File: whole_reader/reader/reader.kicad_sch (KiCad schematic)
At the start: 66 parts, among them U1 LM386, U2 STM32F103C8T6, U3 MCP16301Hx-xCH, U4 MAX3232, Y1 16MHz

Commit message: changed diodes
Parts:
- removed D5, D6: BAT60A, Diode_SMD:D_SOD-323, symbol Diode:BAT60A
- added D5, D6: BAT54J, Diode_SMD:D_SOD-323F, symbol Diode:BAT54J
- D1: value BAT60A -> BAT54J; footprint Diode_SMD:D_SOD-323 -> Diode_SMD:D_SOD-323F
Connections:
- net BOOT0: now also D6.1 (K)
- net V+: now also D5.1 (K)
- net at RJ12.6: now also D6.2 (A)
- net at RJ12.2: now also D5.2 (A)
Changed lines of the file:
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@@
 	(wire
 		(pts
+			(xy 233.68 46.99) (xy 233.68 54.61)
+		)
+		(stroke
+			(width 0)
+			(type default)
+		)
+	)
+	(wire
+		(pts
 			(xy 176.53 130.81) (xy 176.53 134.62)
 		)
@@
 	(wire
 		(pts
-			(xy 233.68 46.99) (xy 233.68 54.61)
-		)
-		(stroke
-			(width 0)
-			(type default)
-		)
-	)
-	(wire
-		(pts
 			(xy 39.37 97.79) (xy 49.53 97.79)
 		)
@@
 	(wire
 		(pts
+			(xy 254 64.77) (xy 255.27 64.77)
+		)
+		(stroke
+			(width 0)
+			(type default)
+		)
+	)
+	(wire
+		(pts
 			(xy 172.72 147.32) (xy 172.72 132.08)
 		)
@@
 	(wire
 		(pts
-			(xy 255.27 64.77) (xy 254 64.77)
-		)
-		(stroke
-			(width 0)
-			(type default)
-		)
-	)
-	(wire
-		(pts
 			(xy 247.65 99.06) (xy 247.65 105.41)
 		)
@@
 	)
 	(symbol
+		(lib_id "Diode:BAT54J")
+		(at 233.68 43.18 270)
+		(unit 1)
+		(exclude_from_sim no)
+		(in_bom yes)
+		(on_board yes)
+		(dnp no)
+		(fields_autoplaced yes)
+		(property "Reference" "D5"
+			(at 236.22 41.5924 90)
+			(effects
+				(font
+					(size 1.27 1.27)
+				)
+				(justify left)
+			)
+		)
+		(property "Value" "BAT54J"
+			(at 236.22 44.1324 90)
+			(effects
+				(font
+					(size 1.27 1.27)
+				)
+				(justify left)
+			)
+		)
+		(property "Footprint" "Diode_SMD:D_SOD-323F"
+			(at 229.235 43.18 0)
+			(effects
+				(font
+					(size 1.27 1.27)
+				)
+				(hide yes)
+			)
+		)
+		(property "Datasheet" "https://assets.nexperia.com/documents/data-sheet/BAT54J.pdf"
+			(at 233.68 43.18 0)
+			(effects
+				(font
+					(size 1.27 1.27)
+				)
+				(hide yes)
+			)
+		)
+		(property "Description" "30V 200mA Schottky diode, SOD-323F"
+			(at 233.68 43.18 0)
+			(effects
+				(font
+					(size 1.27 1.27)
+				)
+				(hide yes)
+			)
+		)
+		(pin "2"
+		)
+		(pin "1"
+		)
+		(instances
+			(project ""
+				(path "/6275a1a7-d424-4390-b849-2e49b1a9780b"
+					(reference "D5")
+					(unit 1)
+				)
+			)
+		)
+	)
+	(symbol
 		(lib_id "power:GND")
 		(at 68.58 67.31 0)
@@
 	)
 	(symbol
-		(lib_id "Diode:BAT54J")
-		(at 140.97 132.08 0)
-		(unit 1)
-		(exclude_from_sim no)
-		(in_bom yes)
-		(on_board yes)
-		(dnp no)
-		(property "Reference" "D1"
-			(at 144.272 130.556 0)
-			(effects
-				(font
-					(size 1.27 1.27)
-				)
-			)
-		)
-		(property "Value" "BAT60A"
-			(at 140.6525 128.27 0)
-			(effects
-				(font
-					(size 1.27 1.27)
-				)
-			)
-		)
-		(property "Footprint" "Diode_SMD:D_SOD-323"
-			(at 140.97 136.525 0)
-			(effects
-				(font
-					(size 1.27 1.27)
-				)
-				(hide yes)
-			)
-		)
-		(property "Datasheet" "https://assets.nexperia.com/documents/data-sheet/BAT54J.pdf"
-			(at 140.97 132.08 0)
-			(effects
-				(font
-					(size 1.27 1.27)
-				)
-				(hide yes)
-			)
-		)
-		(property "Description" "30V 200mA Schottky diode, SOD-323F"
-			(at 140.97 132.08 0)
-			(effects
-				(font
-					(size 1.27 1.27)
-				)
-				(hide yes)
-			)
-		)
-		(property "Note" ""
-			(at 140.97 132.08 0)
-			(effects
-				(font
-					(size 1.27 1.27)
-				)
-			)
-		)
-		(pin "1"
-		)
-		(pin "2"
-		)
-		(instances
-			(project "reader"
-				(path "/6275a1a7-d424-4390-b849-2e49b1a9780b"
-					(reference "D1")
-					(unit 1)
-				)
-			)
-		)
-	)
-	(symbol
 		(lib_id "Device:R")
 		(at 41.91 31.75 0)
@@
 	)
 	(symbol
-		(lib_id "Diode:BAT60A")
-		(at 250.19 64.77 0)
-		(unit 1)
-		(exclude_from_sim no)
-		(in_bom yes)
-		(on_board yes)
-		(dnp no)
-		(property "Reference" "D6"
-			(at 250.19 70.612 0)
-			(effects
-				(font
-					(size 1.27 1.27)
-				)
-			)
-		)
-		(property "Value" "BAT60A"
-			(at 250.19 68.072 0)
-			(effects
-				(font
-					(size 1.27 1.27)
-				)
-			)
-		)
-		(property "Footprint" "Diode_SMD:D_SOD-323"
-			(at 250.19 69.215 0)
-			(effects
-				(font
-					(size 1.27 1.27)
-				)
-				(hide yes)
-			)
-		)
-		(property "Datasheet" "https://www.infineon.com/dgdl/Infineon-BAT60ASERIES-DS-v01_01-en.pdf?fileId=db3a304313d846880113def70c9304a9"
-			(at 250.19 64.77 0)
-			(effects
-				(font
-					(size 1.27 1.27)
-				)
-				(hide yes)
-			)
-		)
-		(property "Description" "10V 3A High Current Recitifier Schottky Diode, SOD-323"
-			(at 250.19 64.77 0)
-			(effects
-				(font
-					(size 1.27 1.27)
-				)
-				(hide yes)
-			)
-		)
-		(property "Note" ""
-			(at 250.19 64.77 0)
-			(effects
-				(font
-					(size 1.27 1.27)
-				)
-			)
-		)
-		(pin "2"
-		)
-		(pin "1"
-		)
-		(instances
-			(project "reader"
-				(path "/6275a1a7-d424-4390-b849-2e49b1a9780b"
-					(reference "D6")
-					(unit 1)
-				)
-			)
-		)
-	)
-	(symbol
 		(lib_id "power:GND")
 		(at 105.41 102.87 0)
@@
 	)
 	(symbol
-		(lib_id "Diode:BAT60A")
-		(at 233.68 43.18 270)
+		(lib_id "Diode:BAT54J")
+		(at 140.97 132.08 0)
 		(unit 1)
 		(exclude_from_sim no)
@@
 		(dnp no)
 		(fields_autoplaced yes)
-		(property "Reference" "D5"
-			(at 236.22 41.5924 90)
+		(property "Reference" "D1"
+			(at 140.6525 125.73 0)
 			(effects
 				(font
 					(size 1.27 1.27)
 				)
-				(justify left)
 			)
 		)
-		(property "Value" "BAT60A"
-			(at 236.22 44.1324 90)
+		(property "Value" "BAT54J"
+			(at 140.6525 128.27 0)
 			(effects
 				(font
 					(size 1.27 1.27)
 				)
-				(justify left)
 			)
 		)
-		(property "Footprint" "Diode_SMD:D_SOD-323"
-			(at 229.235 43.18 0)
+		(property "Footprint" "Diode_SMD:D_SOD-323F"
+			(at 140.97 136.525 0)
 			(effects
 				(font
@@
 			)
 		)
-		(property "Datasheet" "https://www.infineon.com/dgdl/Infineon-BAT60ASERIES-DS-v01_01-en.pdf?fileId=db3a304313d846880113def70c9304a9"
-			(at 233.68 43.18 0)
+		(property "Datasheet" "https://assets.nexperia.com/documents/data-sheet/BAT54J.pdf"
+			(at 140.97 132.08 0)
 			(effects
 				(font
@@
 			)
 		)
-		(property "Description" "10V 3A High Current Recitifier Schottky Diode, SOD-323"
-			(at 233.68 43.18 0)
+		(property "Description" "30V 200mA Schottky diode, SOD-323F"
+			(at 140.97 132.08 0)
 			(effects
 				(font
@@
 			)
 		)
-		(property "Note" ""
-			(at 233.68 43.18 0)
-			(effects
-				(font
-					(size 1.27 1.27)
-				)
-			)
-		)
 		(pin "2"
 		)
@@
 		)
 		(instances
-			(project "reader"
+			(project ""
 				(path "/6275a1a7-d424-4390-b849-2e49b1a9780b"
-					(reference "D5")
+					(reference "D1")
 					(unit 1)
 				)
@@
 					(unit 1)
 				)
+			)
+		)
+	)
+	(symbol
+		(lib_id "Diode:BAT54J")
+		(at 250.19 64.77 0)
+		(unit 1)
+		(exclude_from_sim no)
+		(in_bom yes)
+		(on_board yes)
+		(dnp no)
+		(fields_autoplaced yes)
+		(property "Reference" "D6"
+			(at 249.8725 58.42 0)
+			(effects
+				(font
+					(size 1.27 1.27)
+				)
+			)
+		)
+		(property "Value" "BAT54J"
+			(at 249.8725 60.96 0)
+			(effects
+				(font
+					(size 1.27 1.27)
+				)
+			)
+		)
+		(property "Footprint" "Diode_SMD:D_SOD-323F"
+			(at 250.19 69.215 0)
+			(effects
+				(font
+					(size 1.27 1.27)
+				)
+				(hide yes)
+			)
+		)
+		(property "Datasheet" "https://assets.nexperia.com/documents/data-sheet/BAT54J.pdf"
+			(at 250.19 64.77 0)
+			(effects
+				(font
+					(size 1.27 1.27)
+				)
+				(hide yes)
+			)
+		)
+		(property "Description" "30V 200mA Schottky diode, SOD-323F"
+			(at 250.19 64.77 0)
+			(effects
+				(font
+					(size 1.27 1.27)
+				)
+				(hide yes)
+			)
+		)
+		(pin "2"
+		)
+		(pin "1"
+		)
+		(instances
+			(project ""
+				(path "/6275a1a7-d424-4390-b849-2e49b1a9780b"
+					(reference "D6")
+					(unit 1)
+				)

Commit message: added new diodes
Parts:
- removed D1, D5, D6: BAT54J, Diode_SMD:D_SOD-323F, symbol Diode:BAT54J
- removed D4: BAT60A, Diode_SMD:D_SOD-323, symbol Diode:BAT60A
- added D1, D4, D5, D6: PMEG2010ER, Diode_SMD:Nexperia_CFP3_SOD-123W, symbol Device:D_Schottky
- U1: value LM386 -> LM386M-1
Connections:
- net +3.3V: now also D1.2 (A)
- net BOOT0: now also D6.1 (K)
- net V+: now also D1.1 (K), D4.1 (K), D5.1 (K)
- net at RJ12.2: now also D5.2 (A)
- net at USB-C1.A4 (VBUS), USB-C1.A9 (VBUS), USB-C1.B4 (VBUS)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: now also D4.2 (A)
- net at RJ12.6: now also D6.2 (A)

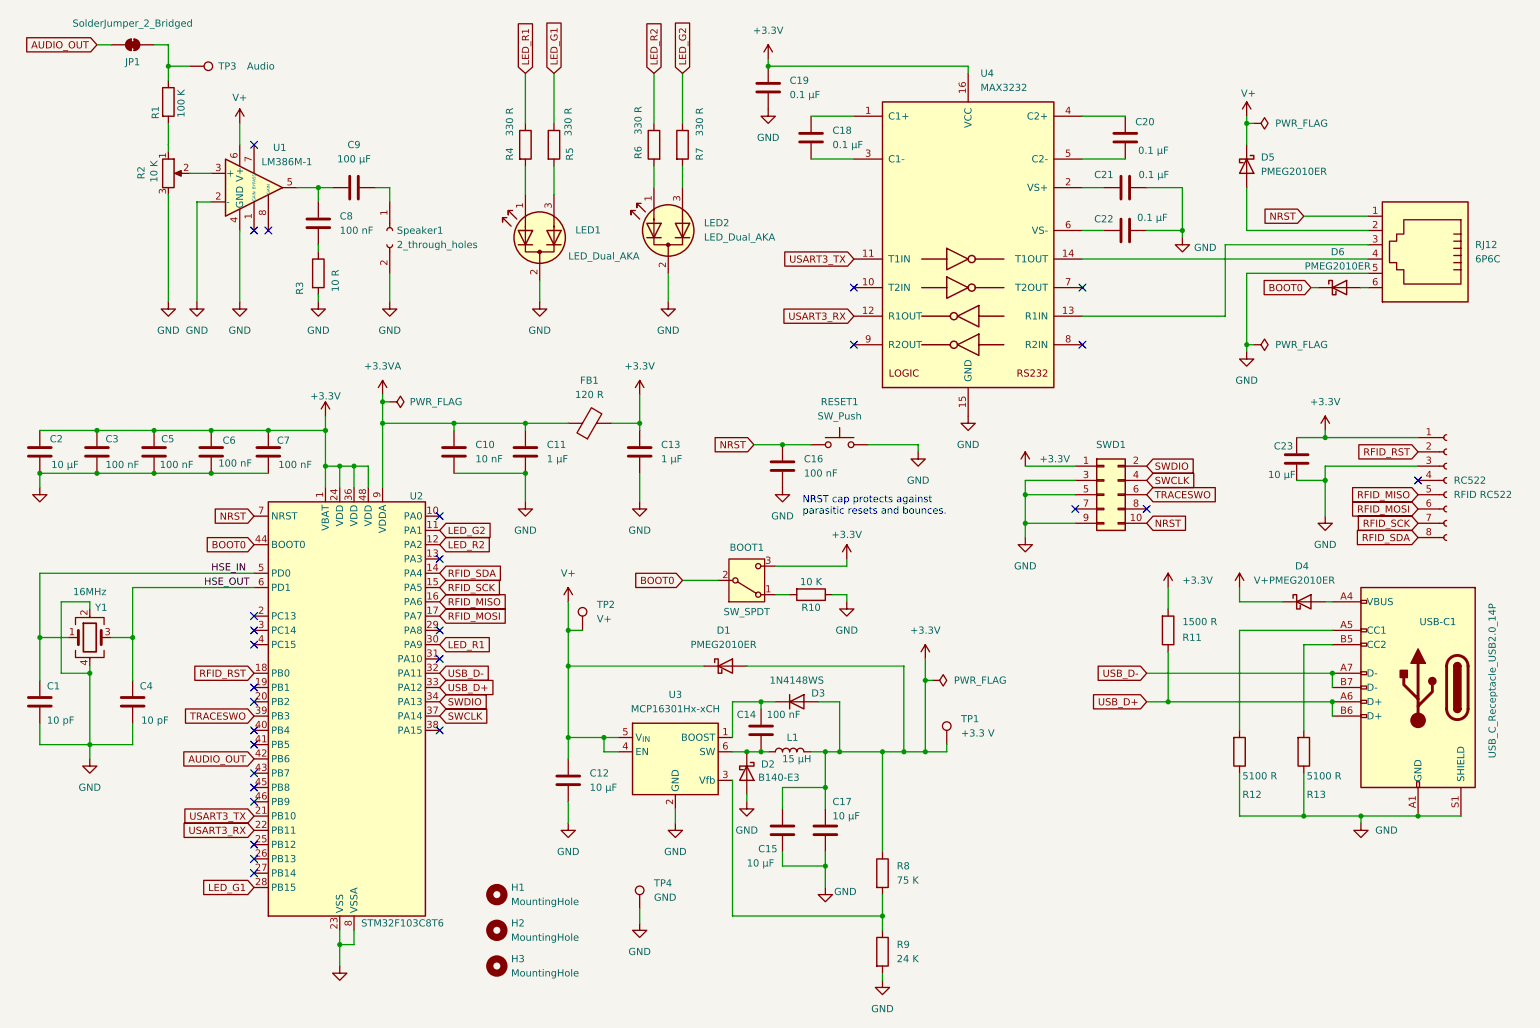
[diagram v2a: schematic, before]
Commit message: Úprava rozloženia dosky a pridanie TP5 pre RFID_IRQ
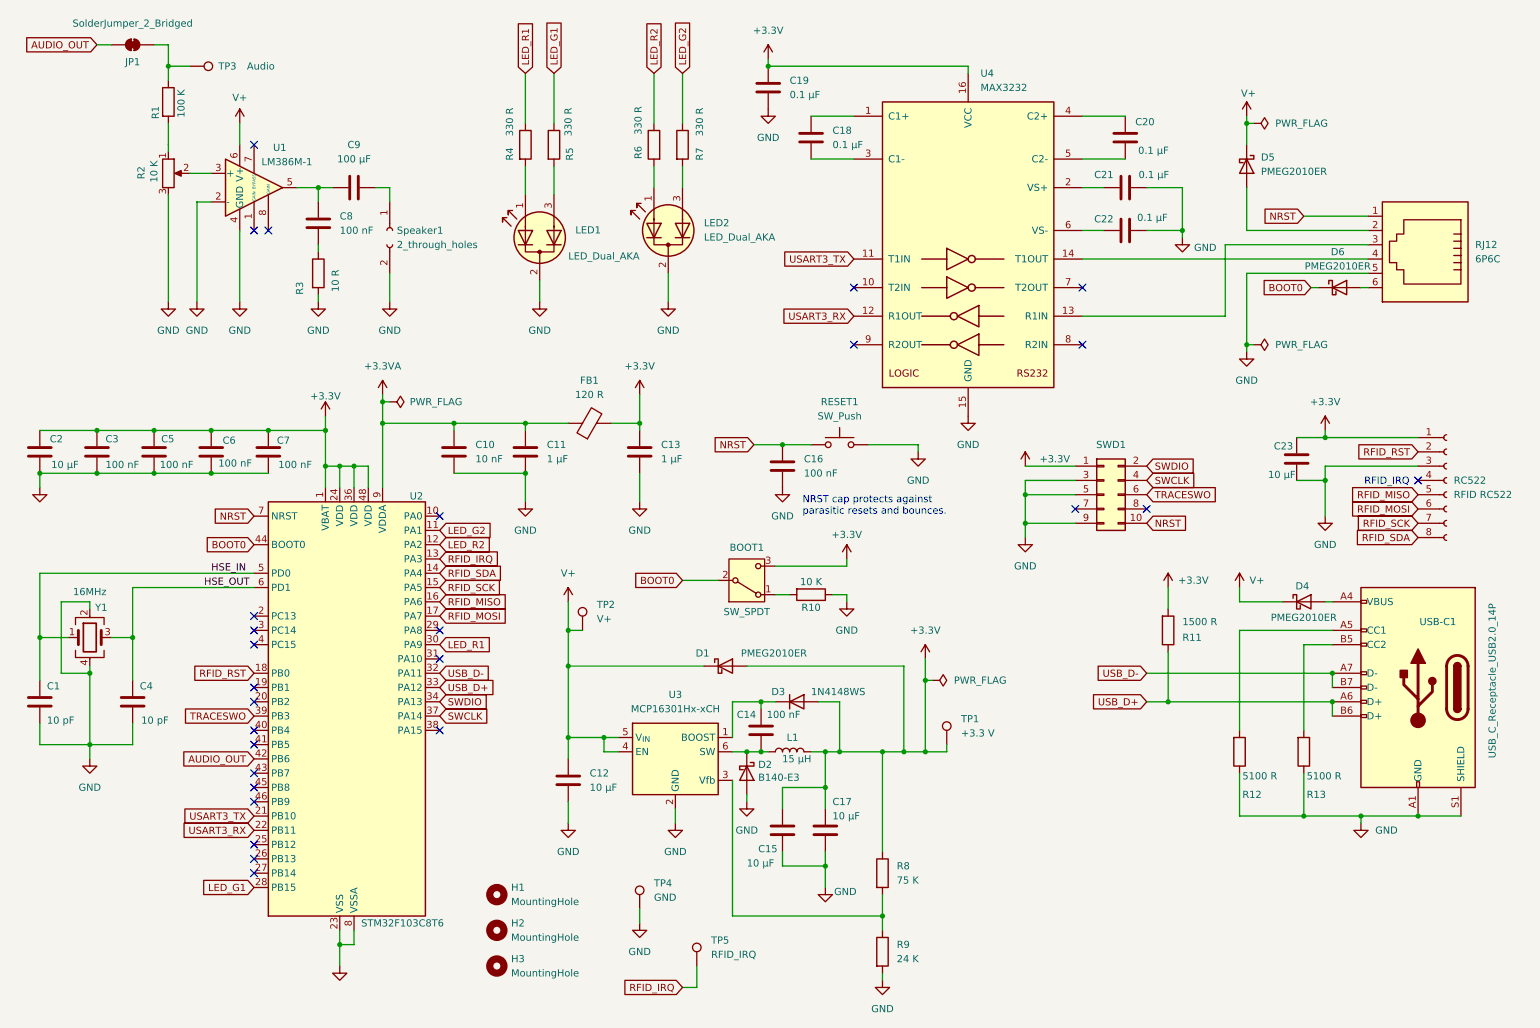
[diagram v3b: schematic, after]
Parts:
- added TP5: RFID_IRQ, TestPoint:TestPoint_THTPad_D1.0mm_Drill0.5mm, symbol Connector:TestPoint
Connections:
- net RFID_IRQ: now reaches U2.13 (PA3)
- net RFID_IRQ: now also TP5.1
- no-connect marks 28 -> 27
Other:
- note added: "RFID_IRQ"
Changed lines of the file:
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@@
 		)
 	)
+	(text "RFID_IRQ"
+		(exclude_from_sim no)
+		(at 262.636 99.314 0)
+		(effects
+			(font
+				(size 1.27 1.27)
+			)
+			(justify right)
+		)
+	)
 	(junction
 		(at 158.75 167.64)
@@
 	)
 	(no_connect
-		(at 90.17 113.03)
-	)
-	(no_connect
 		(at 57.15 39.37)
 	)
@@
 	(wire
 		(pts
+			(xy 133.35 189.23) (xy 135.89 189.23)
+		)
+		(stroke
+			(width 0)
+			(type default)
+		)
+	)
+	(wire
+		(pts
 			(xy 248.92 135.89) (xy 248.92 133.35)
 		)
@@
 	(wire
 		(pts
+			(xy 135.89 189.23) (xy 135.89 185.42)
+		)
+		(stroke
+			(width 0)
+			(type default)
+		)
+	)
+	(wire
+		(pts
 			(xy 151.13 92.71) (xy 156.21 92.71)
 		)
@@
 		)
 	)
+	(global_label "RFID_IRQ"
+		(shape input)
+		(at 90.17 113.03 0)
+		(fields_autoplaced yes)
+		(effects
+			(font
+				(size 1.27 1.27)
+			)
+			(justify left)
+		)
+		(property "Intersheetrefs" "${INTERSHEET_REFS}"
+			(at 101.5615 113.03 0)
+			(effects
+				(font
+					(size 1.27 1.27)
+				)
+				(justify left)
+				(hide yes)
+			)
+		)
+	)
 	(global_label "BOOT0"
 		(shape input)
@@
 		)
 	)
+	(global_label "RFID_IRQ"
+		(shape input)
+		(at 133.35 189.23 180)
+		(fields_autoplaced yes)
+		(effects
+			(font
+				(size 1.27 1.27)
+			)
+			(justify right)
+		)
+		(property "Intersheetrefs" "${INTERSHEET_REFS}"
+			(at 121.9585 189.23 0)
+			(effects
+				(font
+					(size 1.27 1.27)
+				)
+				(justify right)
+				(hide yes)
+			)
+		)
+	)
 	(symbol
 		(lib_id "Diode:1N4148WS")
@@
 		(dnp no)
 		(property "Reference" "D3"
-			(at 157.48 136.906 0)
+			(at 150.368 136.652 0)
 			(effects
 				(font
@@
 		)
 		(property "Value" "1N4148WS"
-			(at 153.67 134.62 0)
+			(at 161.036 136.652 0)
 			(effects
 				(font
@@
 		(dnp no)
 		(property "Reference" "D2"
-			(at 147.32 149.5424 90)
+			(at 146.812 149.606 90)
 			(effects
 				(font
@@
 		(on_board yes)
 		(dnp no)
-		(fields_autoplaced yes)
 		(property "Reference" "#PWR034"
 			(at 232.41 121.92 0)
@@
 		)
 		(property "Value" "V+"
-			(at 234.95 116.8399 0)
+			(at 234.188 116.84 0)
 			(effects
 				(font
@@
 	)
 	(symbol
+		(lib_id "Connector:TestPoint")
+		(at 135.89 185.42 0)
+		(unit 1)
+		(exclude_from_sim no)
+		(in_bom yes)
+		(on_board yes)
+		(dnp no)
+		(fields_autoplaced yes)
+		(property "Reference" "TP5"
+			(at 138.43 180.8479 0)
+			(effects
+				(font
+					(size 1.27 1.27)
+				)
+				(justify left)
+			)
+		)
+		(property "Value" "RFID_IRQ"
+			(at 138.43 183.3879 0)
+			(effects
+				(font
+					(size 1.27 1.27)
+				)
+				(justify left)
+			)
+		)
+		(property "Footprint" "TestPoint:TestPoint_THTPad_D1.0mm_Drill0.5mm"
+			(at 140.97 185.42 0)
+			(effects
+				(font
+					(size 1.27 1.27)
+				)
+				(hide yes)
+			)
+		)
+		(property "Datasheet" "~"
+			(at 140.97 185.42 0)
+			(effects
+				(font
+					(size 1.27 1.27)
+				)
+				(hide yes)
+			)
+		)
+		(property "Description" "test point"
+			(at 135.89 185.42 0)
+			(effects
+				(font
+					(size 1.27 1.27)
+				)
+				(hide yes)
+			)
+		)
+		(pin "1"
+		)
+		(instances
+			(project "reader"
+				(path "/6275a1a7-d424-4390-b849-2e49b1a9780b"
+					(reference "TP5")
+					(unit 1)
+				)
+			)
+		)
+	)
+	(symbol
 		(lib_id "power:+3.3VA")
 		(at 194.31 96.52 0)
@@
 		(on_board yes)
 		(dnp no)
-		(fields_autoplaced yes)
 		(property "Reference" "#PWR032"
 			(at 219.71 121.92 0)
@@
 		)
 		(property "Value" "+3.3V"
-			(at 222.25 116.8399 0)
+			(at 221.488 116.84 0)
 			(effects
 				(font
@@
 		(on_board yes)
 		(dnp no)
-		(fields_autoplaced yes)
 		(property "Reference" "D4"
-			(at 243.5225 114.3 0)
+			(at 243.586 117.856 0)
 			(effects
 				(font
@@
 		)
 		(property "Value" "PMEG2010ER"
-			(at 243.5225 116.84 0)
+			(at 243.84 123.444 0)
 			(effects
 				(font
@@
 		(on_board yes)
 		(dnp no)
-		(fields_autoplaced yes)
 		(property "Reference" "D1"
-			(at 140.6525 125.73 0)
+			(at 136.906 129.794 0)
 			(effects
 				(font
@@
 		)
 		(property "Value" "PMEG2010ER"
-			(at 140.6525 128.27 0)
+			(at 149.606 129.794 0)
 			(effects
 				(font
